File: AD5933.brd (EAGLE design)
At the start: 82.8 x 53.3 mm, 80 parts, among them U1 ADG1604BRUZ, U10 ADP3303ARZ-3.3, U11 AD5242BRZ1M, U12 AD5245BRJZ100-R2, U2 AD5933YRSZ, U3 AD5242BRZ1M, U4 AD8606ARZ, U5 ADG1604BRUZ, U7 AD8606ARZ, U8 LTC6904MPMS8TRPBF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

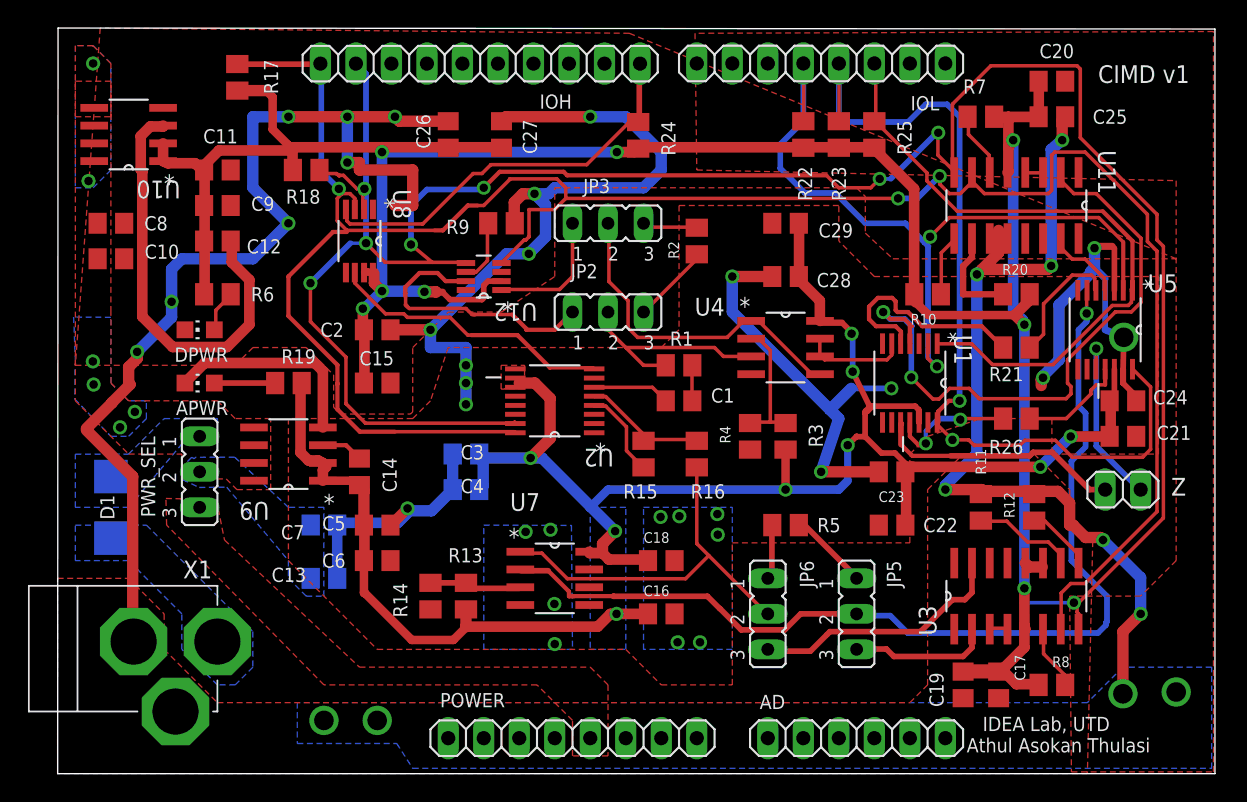
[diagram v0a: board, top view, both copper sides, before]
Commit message: Fix ad8606 wiring bug rev 1.1
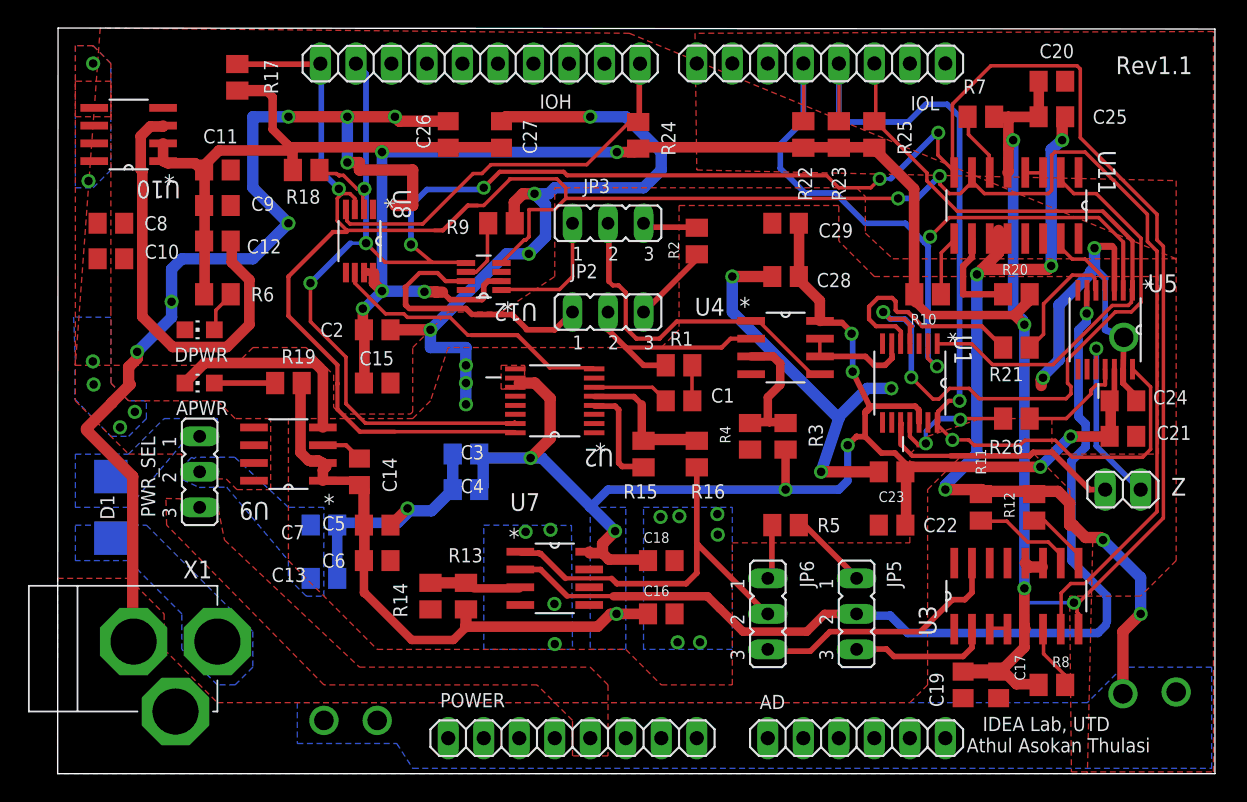
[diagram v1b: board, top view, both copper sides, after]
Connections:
- removed net U4_INA+: JP2.2, R1.2, U4.3
- removed net U4_INA-: R3.1, R4.2, U4.2
- new net U4_INA++: R3.1, R4.2, U4.3
- new net U4_INA--: JP2.2, R1.2, U4.2
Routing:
- net U4_INA+: track 15.7 -> 0.00 mm
- net U4_INA--: track 0.00 -> 15.7 mm
- net U4_INA++: track 0.00 -> 9.50 mm
- net U4_INA-: track 9.46 -> 0.00 mm
- net U2_RFB: track 6.37 -> 7.70 mm
- net U2_VIN: track 9.08 -> 10.3 mm
- net U7_OUTA: track 27.6 -> 28.6 mm
- net U4_OUTB: track 7.45 -> 8.06 mm
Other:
- board text added: "Rev1.1"
- board text removed: "CIMD v1"

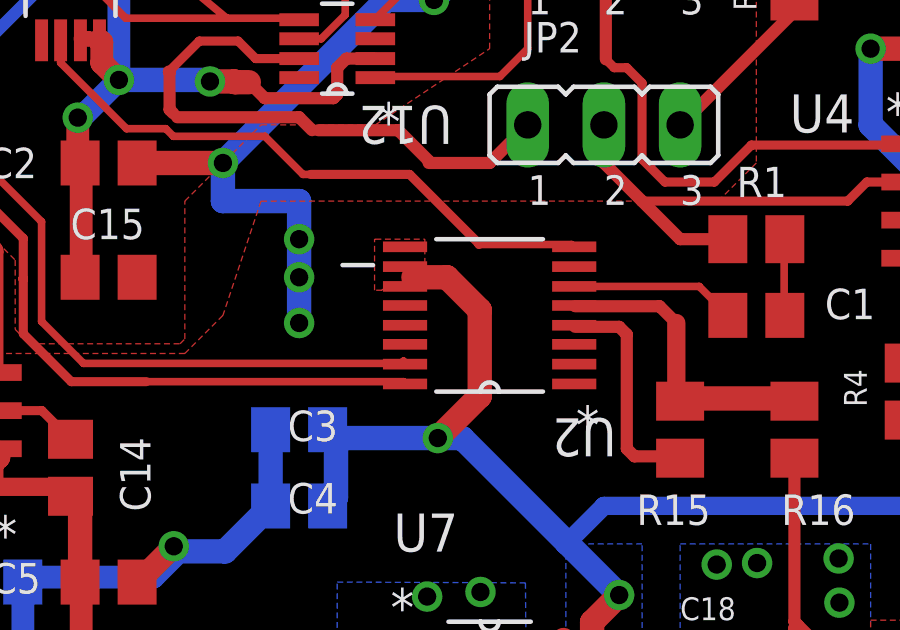
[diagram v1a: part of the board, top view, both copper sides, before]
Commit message: Increase AD5933 pad length
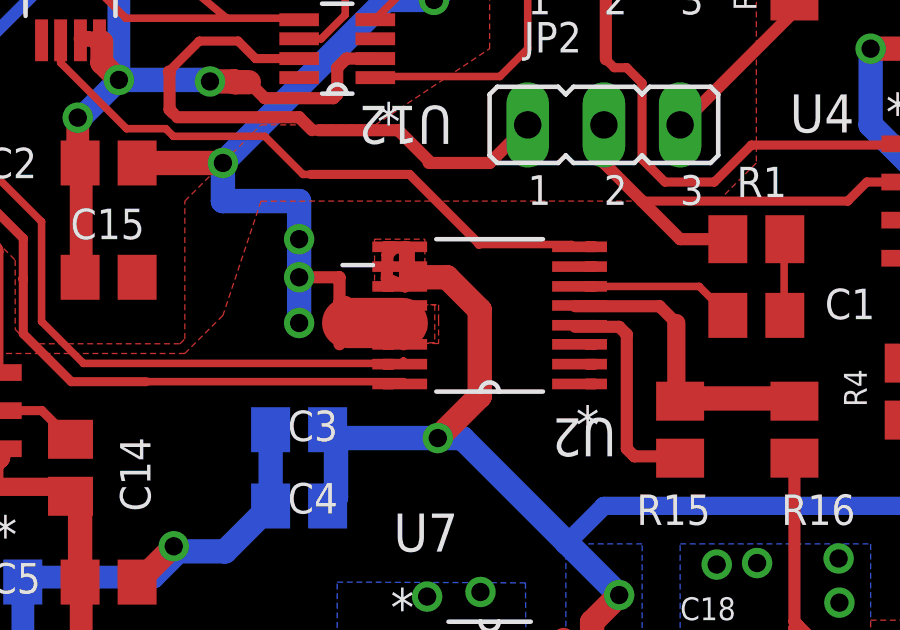
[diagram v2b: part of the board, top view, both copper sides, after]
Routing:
- net AGND: track 92.1 -> 100.5 mm
- net VCC: track 150.2 -> 154.5 mm
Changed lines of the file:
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@@
 <setting verticaltext="up"/>
 </settings>
-<grid distance="0.005" unitdist="inch" unit="inch" style="lines" multiple="1" display="no" altdistance="0.001" altunitdist="inch" altunit="inch"/>
+<grid distance="0.001" unitdist="inch" unit="inch" style="lines" multiple="1" display="no" altdistance="0.0025" altunitdist="inch" altunit="inch"/>
 <layers>
 <layer number="1" name="Top" color="4" fill="1" visible="yes" active="yes"/>
@@
 <wire x1="55.88" y1="25.527" x2="57.912" y2="27.559" width="0.8128" layer="16"/>
 <wire x1="57.912" y1="27.559" x2="59.6392" y2="27.559" width="0.8128" layer="16"/>
+<wire x1="32.7406" y1="26.3398" x2="32.7406" y2="27.0002" width="0.4064" layer="1"/>
+<wire x1="29.21" y1="27.94" x2="30.5562" y2="27.94" width="0.4064" layer="1"/>
+<wire x1="30.5562" y1="27.94" x2="30.5562" y2="27.1018" width="0.4064" layer="1"/>
+<wire x1="30.5562" y1="27.1018" x2="30.7848" y2="27.1018" width="0.4064" layer="1"/>
+<wire x1="30.7848" y1="27.1018" x2="30.7848" y2="26.797" width="0.4064" layer="1"/>
+<wire x1="32.7406" y1="27.0002" x2="32.6898" y2="27.0002" width="0.4064" layer="1"/>
+<wire x1="32.6898" y1="27.0002" x2="32.6898" y2="25.7048" width="0.4064" layer="1"/>
+<wire x1="30.5562" y1="26.162" x2="30.5562" y2="27.1018" width="0.4064" layer="1"/>
+<polygon width="0.4064" layer="1" orphans="yes" thermals="no" rank="2">
+<vertex x="33.7312" y="27.0256"/>
+<vertex x="33.7312" y="25.7556"/>
+<vertex x="30.7594" y="25.7556"/>
+<vertex x="30.7594" y="26.0096"/>
+<vertex x="30.7594" y="27.0002"/>
+</polygon>
+<polygon width="0.4064" layer="1" rank="2">
+<vertex x="30.7086" y="27.0256"/>
+<vertex x="33.8582" y="27.0256"/>
+<vertex x="33.8582" y="26.5176"/>
+<vertex x="33.8582" y="25.7302"/>
+<vertex x="30.7848" y="25.8064"/>
+<vertex x="30.7086" y="25.8064"/>
+<vertex x="30.7086" y="27.0002"/>
+</polygon>
+<wire x1="30.5562" y1="25.7048" x2="30.5562" y2="26.162" width="0.4064" layer="1"/>
+<wire x1="30.5562" y1="26.162" x2="30.8102" y2="26.416" width="0.4064" layer="1"/>
+<wire x1="30.8102" y1="26.416" x2="32.6644" y2="26.416" width="1.6764" layer="1"/>
+<wire x1="32.6644" y1="26.416" x2="32.7406" y2="26.3398" width="0.4064" layer="1"/>
 </signal>
 <signal name="VDD" class="1">
@@
 <wire x1="61.595" y1="26.035" x2="61.341" y2="26.289" width="0.4064" layer="1"/>
 <wire x1="61.341" y1="26.289" x2="58.293" y2="26.289" width="0.4064" layer="1"/>
+<wire x1="32.7406" y1="27.6352" x2="32.7406" y2="28.2956" width="0.4064" layer="1"/>
+<wire x1="32.7406" y1="28.2956" x2="32.7406" y2="28.956" width="0.4064" layer="1"/>
+<wire x1="32.7406" y1="27.6352" x2="32.131" y2="27.8892" width="0.4064" layer="1"/>
+<wire x1="32.131" y1="27.8892" x2="32.1564" y2="28.702" width="0.4064" layer="1"/>
+<wire x1="32.1564" y1="28.702" x2="32.385" y2="28.9306" width="0.4064" layer="1"/>
+<wire x1="32.385" y1="28.9306" x2="32.8422" y2="28.9306" width="0.4064" layer="1"/>
+<wire x1="32.8422" y1="28.9306" x2="32.8676" y2="28.9052" width="0.4064" layer="1"/>
+<wire x1="32.8676" y1="28.9052" x2="32.8676" y2="28.4226" width="0.4064" layer="1"/>
+<wire x1="32.8676" y1="28.4226" x2="32.7406" y2="28.2956" width="0.4064" layer="1"/>
 </signal>
 <signal name="N$35">
